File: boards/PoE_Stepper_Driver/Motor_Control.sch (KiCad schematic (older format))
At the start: 21 parts, among them J2 Motor, J3 Limits, U15 TMC429-I, U16 TMC2660C-PA

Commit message: finished footprint assignment
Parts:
- C15, C16, C18, C23: footprint (none) -> Capacitor_SMD:C_0805_2012Metric_Pad1.15x1.40mm_HandSolder
- C19, C21: footprint (none) -> Capacitor_THT:CP_Radial_D8.0mm_P3.50mm
- C20, C22: footprint (none) -> Capacitor_SMD:C_1206_3216Metric_Pad1.42x1.75mm_HandSolder
- J3: footprint (none) -> Connector_JST:JST_PH_B4B-PH-K_1x04_P2.00mm_Vertical
- R23, R24, R25, R27, R29: footprint (none) -> Resistor_SMD:R_0805_2012Metric_Pad1.15x1.40mm_HandSolder
- R26, R28: footprint (none) -> Resistor_SMD:R_2010_5025Metric_Pad1.52x2.65mm_HandSolder
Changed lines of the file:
@@
 F 0 "R23" H 1709 3196 50  0000 L CNN
 F 1 "10k" H 1709 3105 50  0000 L CNN
-F 2 "" H 1650 3150 50  0001 C CNN
+F 2 "Resistor_SMD:R_0805_2012Metric_Pad1.15x1.40mm_HandSolder" H 1650 3150 50  0001 C CNN
 F 3 "~" H 1650 3150 50  0001 C CNN
 	1    1650 3150
@@
 F 0 "R24" H 2009 3196 50  0000 L CNN
 F 1 "10k" H 2009 3105 50  0000 L CNN
-F 2 "" H 1950 3150 50  0001 C CNN
+F 2 "Resistor_SMD:R_0805_2012Metric_Pad1.15x1.40mm_HandSolder" H 1950 3150 50  0001 C CNN
 F 3 "~" H 1950 3150 50  0001 C CNN
 	1    1950 3150
@@
 F 0 "R25" H 2284 3196 50  0000 L CNN
 F 1 "10k" H 2284 3105 50  0000 L CNN
-F 2 "" H 2225 3150 50  0001 C CNN
+F 2 "Resistor_SMD:R_0805_2012Metric_Pad1.15x1.40mm_HandSolder" H 2225 3150 50  0001 C CNN
 F 3 "~" H 2225 3150 50  0001 C CNN
 	1    2225 3150
@@
 F 0 "R27" H 6159 3746 50  0000 L CNN
 F 1 "22" H 6159 3655 50  0000 L CNN
-F 2 "" H 6100 3700 50  0001 C CNN
+F 2 "Resistor_SMD:R_0805_2012Metric_Pad1.15x1.40mm_HandSolder" H 6100 3700 50  0001 C CNN
 F 3 "~" H 6100 3700 50  0001 C CNN
 	1    6100 3700
@@
 F 0 "C15" H 6192 3996 50  0000 L CNN
 F 1 "10nF" H 6192 3905 50  0000 L CNN
-F 2 "" H 6100 3950 50  0001 C CNN
+F 2 "Capacitor_SMD:C_0805_2012Metric_Pad1.15x1.40mm_HandSolder" H 6100 3950 50  0001 C CNN
 F 3 "~" H 6100 3950 50  0001 C CNN
 	1    6100 3950
@@
 F 0 "R26" H 5859 3796 50  0000 L CNN
 F 1 "75m" H 5859 3705 50  0000 L CNN
-F 2 "" H 5800 3750 50  0001 C CNN
+F 2 "Resistor_SMD:R_2010_5025Metric_Pad1.52x2.65mm_HandSolder" H 5800 3750 50  0001 C CNN
 F 3 "~" H 5800 3750 50  0001 C CNN
 	1    5800 3750
@@
 F 0 "R29" H 6884 3946 50  0000 L CNN
 F 1 "22" H 6884 3855 50  0000 L CNN
-F 2 "" H 6825 3900 50  0001 C CNN
+F 2 "Resistor_SMD:R_0805_2012Metric_Pad1.15x1.40mm_HandSolder" H 6825 3900 50  0001 C CNN
 F 3 "~" H 6825 3900 50  0001 C CNN
 	1    6825 3900
@@
 F 0 "C16" H 6917 4196 50  0000 L CNN
 F 1 "10nF" H 6917 4105 50  0000 L CNN
-F 2 "" H 6825 4150 50  0001 C CNN
+F 2 "Capacitor_SMD:C_0805_2012Metric_Pad1.15x1.40mm_HandSolder" H 6825 4150 50  0001 C CNN
 F 3 "~" H 6825 4150 50  0001 C CNN
 	1    6825 4150
@@
 F 0 "R28" H 6584 3996 50  0000 L CNN
 F 1 "75m" H 6584 3905 50  0000 L CNN
-F 2 "" H 6525 3950 50  0001 C CNN
+F 2 "Resistor_SMD:R_2010_5025Metric_Pad1.52x2.65mm_HandSolder" H 6525 3950 50  0001 C CNN
 F 3 "~" H 6525 3950 50  0001 C CNN
 	1    6525 3950
@@
 F 0 "C23" V 9396 2950 50  0000 C CNN
 F 1 "470nF" V 9487 2950 50  0000 C CNN
-F 2 "" H 9625 2950 50  0001 C CNN
+F 2 "Capacitor_SMD:C_0805_2012Metric_Pad1.15x1.40mm_HandSolder" H 9625 2950 50  0001 C CNN
 F 3 "~" H 9625 2950 50  0001 C CNN
 	1    9625 2950
@@
 F 0 "C18" H 8325 2475 50  0000 L CNN
 F 1 "220nF" H 8225 2325 50  0000 L CNN
-F 2 "" H 8500 2400 50  0001 C CNN
+F 2 "Capacitor_SMD:C_0805_2012Metric_Pad1.15x1.40mm_HandSolder" H 8500 2400 50  0001 C CNN
 F 3 "~" H 8500 2400 50  0001 C CNN
 	1    8500 2400
@@
 F 0 "C20" V 8950 1775 50  0000 C CNN
 F 1 "10uF" V 9025 1750 50  0000 C CNN
-F 2 "" H 9100 1925 50  0001 C CNN
+F 2 "Capacitor_SMD:C_1206_3216Metric_Pad1.42x1.75mm_HandSolder" H 9100 1925 50  0001 C CNN
 F 3 "~" H 9100 1925 50  0001 C CNN
 	1    9100 1925
@@
 F 0 "C22" V 8950 2400 50  0000 C CNN
 F 1 "10uF" V 9025 2375 50  0000 C CNN
-F 2 "" H 9100 2500 50  0001 C CNN
+F 2 "Capacitor_SMD:C_1206_3216Metric_Pad1.42x1.75mm_HandSolder" H 9100 2500 50  0001 C CNN
 F 3 "~" H 9100 2500 50  0001 C CNN
 	1    9100 2500
@@
 F 0 "C21" V 9250 2350 50  0000 C CNN
 F 1 "100uF" V 9175 2350 50  0000 C CNN
-F 2 "" H 9100 2200 50  0001 C CNN
+F 2 "Capacitor_THT:CP_Radial_D8.0mm_P3.50mm" H 9100 2200 50  0001 C CNN
 F 3 "~" H 9100 2200 50  0001 C CNN
 	1    9100 2200
@@
 F 0 "C19" V 9250 1775 50  0000 C CNN
 F 1 "100uF" V 9175 1800 50  0000 C CNN
-F 2 "" H 9100 1625 50  0001 C CNN
+F 2 "Capacitor_THT:CP_Radial_D8.0mm_P3.50mm" H 9100 1625 50  0001 C CNN
 F 3 "~" H 9100 1625 50  0001 C CNN
 	1    9100 1625
@@
 F 0 "J3" H 1147 3532 50  0000 R CNN
 F 1 "Limits" H 1147 3623 50  0000 R CNN
-F 2 "" H 1175 3650 50  0001 C CNN
+F 2 "Connector_JST:JST_PH_B4B-PH-K_1x04_P2.00mm_Vertical" H 1175 3650 50  0001 C CNN
 F 3 "~" H 1175 3650 50  0001 C CNN
 	1    1175 3650

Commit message: almost finished ethernet layout
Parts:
- added C2: 0.1uF, Capacitor_SMD:C_0805_2012Metric_Pad1.15x1.40mm_HandSolder, symbol device:C_Small
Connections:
- net +12V: now also C2.2
- net GND: now also C2.1
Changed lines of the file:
@@
 	8500 2500 8500 2550
 Wire Wire Line
-	8600 1625 8600 2550
+	8600 1625 8600 1750
 Wire Wire Line
 	8700 1925 8700 2550
@@
 Wire Wire Line
 	1425 3650 1425 3375
+$Comp
+L device:C_Small C?
+U 1 1 623A88DB
+P 8275 1750
+AR Path="/623A88DB" Ref="C?"  Part="1"
+AR Path="/6293177D/623A88DB" Ref="C2"  Part="1"
+F 0 "C2" V 8475 1775 50  0000 L CNN
+F 1 "0.1uF" V 8375 1650 50  0000 L CNN
+F 2 "Capacitor_SMD:C_0805_2012Metric_Pad1.15x1.40mm_HandSolder" H 8275 1750 50  0001 C CNN
+F 3 "~" H 8275 1750 50  0001 C CNN
+	1    8275 1750
+	0    -1   -1   0
+$EndComp
+Wire Wire Line
+	8375 1750 8600 1750
+Connection ~ 8600 1750
+Wire Wire Line
+	8600 1750 8600 2550
+$Comp
+L power:GND #PWR04
+U 1 1 623B63E5
+P 8125 1775
+F 0 "#PWR04" H 8125 1525 50  0001 C CNN
+F 1 "GND" H 8130 1602 50  0000 C CNN
+F 2 "" H 8125 1775 50  0001 C CNN
+F 3 "" H 8125 1775 50  0001 C CNN
+	1    8125 1775
+	1    0    0    -1
+$EndComp
+Wire Wire Line
+	8175 1750 8125 1750
+Wire Wire Line
+	8125 1750 8125 1775
 $EndSCHEMATC

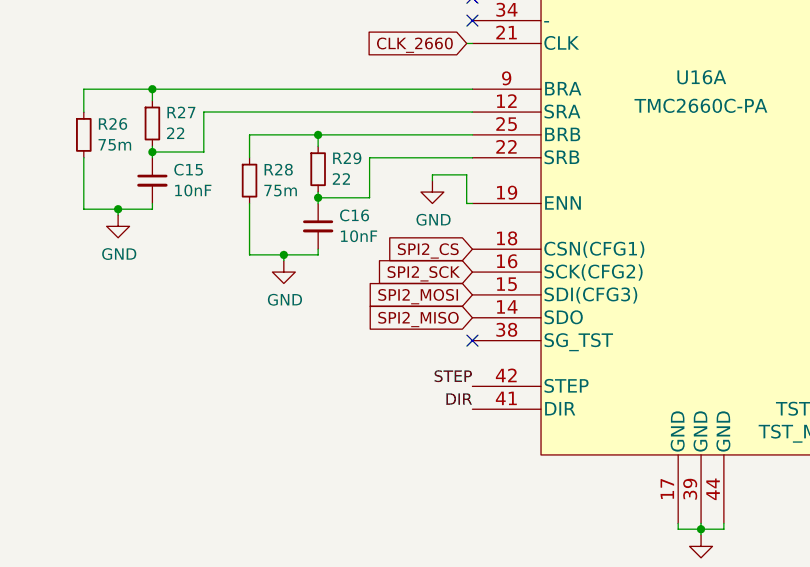
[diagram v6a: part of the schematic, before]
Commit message: added timers for trinamic clks
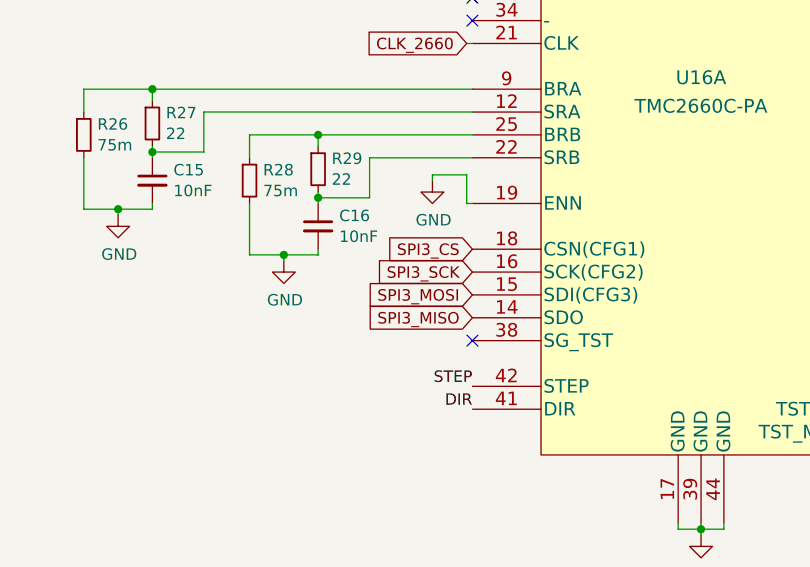
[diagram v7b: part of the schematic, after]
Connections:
- net SPI2_CS renamed SPI3_CS
- net SPI2_MISO renamed SPI3_MISO
- net SPI2_MOSI renamed SPI3_MOSI
- net SPI2_SCK renamed SPI3_SCK
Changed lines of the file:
@@
 CLK_2660
 Text GLabel 7500 4350 0    50   Input ~ 0
-SPI2_SCK
+SPI3_SCK
 Text GLabel 7500 4550 0    50   Input ~ 0
-SPI2_MISO
+SPI3_MISO
 Text GLabel 7500 4450 0    50   Input ~ 0
-SPI2_MOSI
+SPI3_MOSI
 Text GLabel 7500 4250 0    50   Input ~ 0
-SPI2_CS
+SPI3_CS
 $Comp
 L device:R_Small R27
